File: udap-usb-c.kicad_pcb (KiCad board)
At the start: 2 copper layers, 25 x 10 mm, 25 parts, among them J201 Conn_02x04_Counter_Clockwise, P1 USB_C_Plug, U2 MIC5245-3.3YM5, U201 NUF6401MNT1, U202 STM32F042F6Px, U4 NUF2042XV6T1G

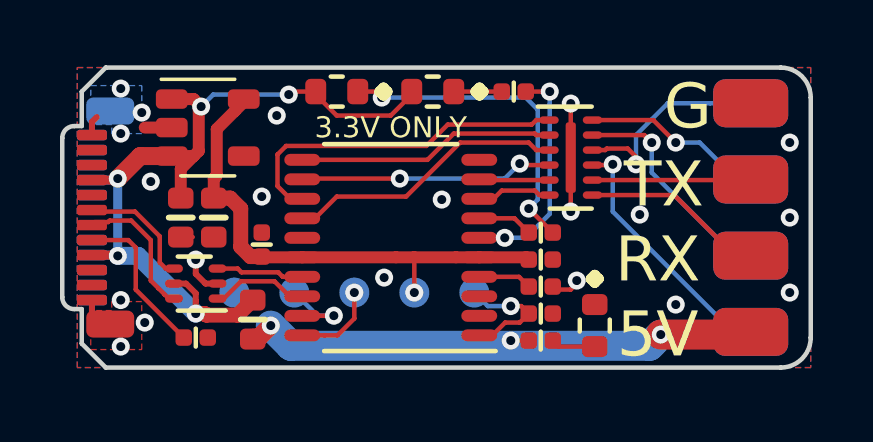
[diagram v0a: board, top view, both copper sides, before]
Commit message: Spaced 4.7u apart more, now easier to solder
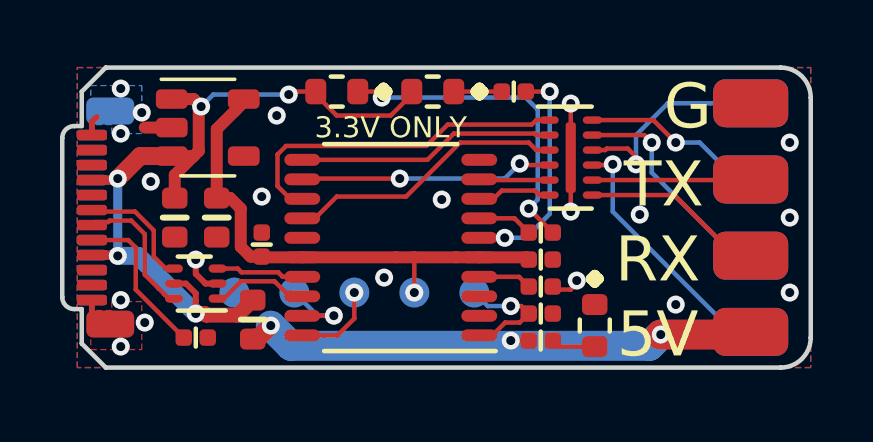
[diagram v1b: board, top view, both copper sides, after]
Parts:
- moved C2 0.20 mm to (93.3, 106.0)
- moved C5 0.10 mm to (94.7, 106.0)
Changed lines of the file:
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@@
     (thickness 0.7)
     (drawings 30)
-    (tracks 265)
+    (tracks 262)
     (zones 0)
     (modules 25)
@@
   )
   (module passive:C_0603 (layer F.Cu)
-    (at 94.6 106 270)
+    (at 94.7 106 270)
     (descr "Capacitor SMD 0603 (1608 Metric), square (rectangular) end terminal, IPC_7351 nominal, (Body size source: http://www.tortai-tech.com/upload/download/2011102023233369053.pdf), generated with kicad-footprint-generator")
     (tags capacitor)
@@
   )
   (module passive:C_0603 (layer F.Cu)
-    (at 93.5 106 270)
+    (at 93.3 106 270)
     (descr "Capacitor SMD 0603 (1608 Metric), square (rectangular) end terminal, IPC_7351 nominal, (Body size source: http://www.tortai-tech.com/upload/download/2011102023233369053.pdf), generated with kicad-footprint-generator")
     (tags capacitor)
@@
   (segment (start 105.025 107.325) (end 105.1 107.4) (width 0.4) (layer F.Cu) (net 1))
   (segment (start 103.45 107.325) (end 105.025 107.325) (width 0.4) (layer F.Cu) (net 1))
-  (segment (start 94.7 104.6) (end 94.7 103.05) (width 0.4) (layer F.Cu) (net 1))
-  (segment (start 94.7 103.05) (end 95.30429 102.44571) (width 0.4) (layer F.Cu) (net 1))
-  (segment (start 94.6 105.35) (end 94.6 104.7) (width 0.4) (layer F.Cu) (net 1))
-  (segment (start 95.30429 102.44571) (end 95.7 102.05) (width 0.4) (layer F.Cu) (net 1))
-  (segment (start 94.6 104.7) (end 94.7 104.6) (width 0.4) (layer F.Cu) (net 1))
-  (segment (start 95.825 107.3) (end 96.2 107.3) (width 0.5) (layer F.Cu) (net 1))
-  (segment (start 95.5 106.975) (end 95.825 107.3) (width 0.5) (layer F.Cu) (net 1))
-  (segment (start 94.6 105.35) (end 95.15 105.35) (width 0.5) (layer F.Cu) (net 1))
-  (segment (start 95.5 105.7) (end 95.5 106.975) (width 0.5) (layer F.Cu) (net 1))
-  (segment (start 95.15 105.35) (end 95.5 105.7) (width 0.5) (layer F.Cu) (net 1))
   (segment (start 101.2855 107.3307) (end 101.2798 107.325) (width 0.15) (layer F.Cu) (net 1))
   (segment (start 101.2855 108.5) (end 101.2855 107.3307) (width 0.15) (layer F.Cu) (net 1))
   (segment (start 100.675 107.325) (end 101.2798 107.325) (width 0.4) (layer F.Cu) (net 1))
   (segment (start 101.2798 107.325) (end 102.675 107.325) (width 0.4) (layer F.Cu) (net 1))
+  (segment (start 95.30429 102.44571) (end 95.7 102.05) (width 0.4) (layer F.Cu) (net 1))
+  (segment (start 94.7 103.05) (end 95.30429 102.44571) (width 0.4) (layer F.Cu) (net 1))
+  (segment (start 94.7 105.35) (end 94.7 103.05) (width 0.4) (layer F.Cu) (net 1))
+  (segment (start 95.825 107.3) (end 95.5 106.975) (width 0.4) (layer F.Cu) (net 1))
+  (segment (start 96.2 107.3) (end 95.825 107.3) (width 0.4) (layer F.Cu) (net 1))
+  (segment (start 95.5 105.7) (end 95.15 105.35) (width 0.4) (layer F.Cu) (net 1))
+  (segment (start 95.15 105.35) (end 94.7 105.35) (width 0.4) (layer F.Cu) (net 1))
+  (segment (start 95.5 106.975) (end 95.5 105.7) (width 0.4) (layer F.Cu) (net 1))
   (via (at 91.5 101.7) (size 0.6) (drill 0.3) (layers F.Cu B.Cu) (net 2))
   (via (at 91.5 108.75) (size 0.6) (drill 0.3) (layers F.Cu B.Cu) (net 2))
@@
   (segment (start 94.725 108.2) (end 94.325 108.2) (width 0.2) (layer F.Cu) (net 2))
   (segment (start 94.325 108.2) (end 94 107.875) (width 0.2) (layer F.Cu) (net 2))
-  (segment (start 93.9 106.65) (end 93.65 106.65) (width 0.15) (layer F.Cu) (net 2))
   (via (at 113.8 103.5) (size 0.6) (drill 0.3) (layers F.Cu B.Cu) (net 2))
   (via (at 113.8 106) (size 0.6) (drill 0.3) (layers F.Cu B.Cu) (net 2))
@@
   (segment (start 93.93 103.95) (end 94.1 103.78) (width 0.4) (layer F.Cu) (net 3))
   (segment (start 94.1 103.78) (end 94.1 102.4) (width 0.4) (layer F.Cu) (net 3))
-  (segment (start 93.5 104.38) (end 93.93 103.95) (width 0.4) (layer F.Cu) (net 3))
-  (segment (start 93.5 105.35) (end 93.5 104.38) (width 0.4) (layer F.Cu) (net 3))
-  (segment (start 92.8 107.5) (end 93 107.7) (width 0.15) (layer F.Cu) (net 4))
-  (segment (start 92.8 106.625721) (end 92.8 107.5) (width 0.15) (layer F.Cu) (net 4))
+  (segment (start 93.3 104.58) (end 93.93 103.95) (width 0.4) (layer F.Cu) (net 3))
+  (segment (start 93.3 105.35) (end 93.3 104.58) (width 0.4) (layer F.Cu) (net 3))
   (segment (start 93 107.7) (end 93.275 107.7) (width 0.15) (layer F.Cu) (net 4))
+  (segment (start 90.59 105.8) (end 91.974279 105.8) (width 0.15) (layer F.Cu) (net 4))
+  (segment (start 91.974279 105.8) (end 92.6 106.425721) (width 0.15) (layer F.Cu) (net 4))
   (segment (start 90.54 105.75) (end 90.59 105.8) (width 0.15) (layer F.Cu) (net 4))
-  (segment (start 91.974279 105.8) (end 92.8 106.625721) (width 0.15) (layer F.Cu) (net 4))
-  (segment (start 90.59 105.8) (end 91.974279 105.8) (width 0.15) (layer F.Cu) (net 4))
+  (segment (start 92.6 106.425721) (end 92.6 107.3) (width 0.15) (layer F.Cu) (net 4))
+  (segment (start 92.6 107.3) (end 93 107.7) (width 0.15) (layer F.Cu) (net 4))
+  (segment (start 91.85 106.1) (end 92.3 106.55) (width 0.15) (layer F.Cu) (net 5))
+  (segment (start 90.63999 106.15001) (end 91.081948 106.15001) (width 0.15) (layer F.Cu) (net 5))
   (segment (start 93.1 108.7) (end 93.275 108.7) (width 0.15) (layer F.Cu) (net 5))
-  (segment (start 92.965011 108.565011) (end 93.1 108.7) (width 0.15) (layer F.Cu) (net 5))
+  (segment (start 92.74999 108.351195) (end 92.963806 108.565011) (width 0.15) (layer F.Cu) (net 5))
   (segment (start 92.963806 108.565011) (end 92.965011 108.565011) (width 0.15) (layer F.Cu) (net 5))
-  (segment (start 92.74999 108.34999) (end 92.74999 108.351195) (width 0.15) (layer F.Cu) (net 5))
-  (segment (start 92.5 108.1) (end 92.74999 108.34999) (width 0.15) (layer F.Cu) (net 5))
-  (segment (start 90.63999 106.15001) (end 91.081948 106.15001) (width 0.15) (layer F.Cu) (net 5))
   (segment (start 91.131958 106.1) (end 91.85 106.1) (width 0.15) (layer F.Cu) (net 5))
   (segment (start 91.081948 106.15001) (end 91.131958 106.1) (width 0.15) (layer F.Cu) (net 5))
+  (segment (start 92.74999 108.34999) (end 92.74999 108.351195) (width 0.15) (layer F.Cu) (net 5))
+  (segment (start 92.965011 108.565011) (end 93.1 108.7) (width 0.15) (layer F.Cu) (net 5))
   (segment (start 90.54 106.25) (end 90.63999 106.15001) (width 0.15) (layer F.Cu) (net 5))
-  (segment (start 92.74999 108.351195) (end 92.963806 108.565011) (width 0.15) (layer F.Cu) (net 5))
-  (segment (start 91.85 106.1) (end 92.5 106.75) (width 0.15) (layer F.Cu) (net 5))
-  (segment (start 92.5 106.75) (end 92.5 108.1) (width 0.15) (layer F.Cu) (net 5))
+  (segment (start 92.3 106.55) (end 92.3 107.9) (width 0.15) (layer F.Cu) (net 5))
+  (segment (start 92.3 107.9) (end 92.74999 108.34999) (width 0.15) (layer F.Cu) (net 5))
   (via (at 96.5 109.6) (size 0.6) (drill 0.3) (layers F.Cu B.Cu) (net 7))
   (via (at 109.5 109.9) (size 0.6) (drill 0.3) (layers F.Cu B.Cu) (net 7))
